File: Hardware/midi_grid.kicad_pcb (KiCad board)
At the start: 2 copper layers, 275 x 200 mm, 329 parts, among them J1 USB_OTG, J2 3.5mm jack, J3 3.5mm jack, J4 Conn_01x04_Male, M1 Mounting_hole, M2 Mounting_hole, M3 Mounting_hole, Q1 BSH205G2, Q10 BSH205G2, Q11 BSH205G2, Q12 BSH205G2, Q13 BSH205G2, Q14 BSH205G2, Q15 BSH205G2, Q16 BSH205G2, Q17 BSH205G2, Q18 BSH205G2, Q19 BSH205G2, Q2 BSH205G2, Q20 BSH205G2, Q21 NX7002AK, Q22 NX7002AK, Q23 NX7002AK, Q24 NX7002AK, Q25 NX7002AK, Q26 NX7002AK, Q27 NX7002AK, Q28 NX7002AK, Q29 NX7002AK, Q3 BSH205G2, Q30 NX7002AK, Q31 NX7002AK, Q32 NX7002AK, Q33 NX7002AK, Q34 NX7002AK, Q4 BSH205G2, Q5 BSH205G2, Q6 BSH205G2, Q7 BSH205G2, Q8 BSH205G2, Q9 BSH205G2, SW1 Button_matrix_4x4, SW10 SW_Push, SW11 SW_Push, SW12 SW_Push, SW13 SW_Push, SW14 SW_Push, SW15 SW_Push, SW16 SW_Push, SW17 SW_Push, SW18 SW_Push, SW19 SW_Push, SW2 Button_matrix_4x4, SW20 SW_Push, SW21 SW_Push, SW22 SW_Push, SW23 SW_Push, SW24 SW_Push, SW25 EC12E24204A9, SW26 EC12E24204A9, SW3 Button_matrix_4x4, SW4 Button_matrix_4x4, SW5 SW_Push, SW6 SW_Push, SW7 SW_Push, SW8 SW_Push, SW9 SW_Push, U1 STM32F411RCT6, U2 74HC138, U3 74HC138, U4 74HC138, U5 USBUF02W6, U6 VO617A, U7 LD1117STR, Y1 8MHz

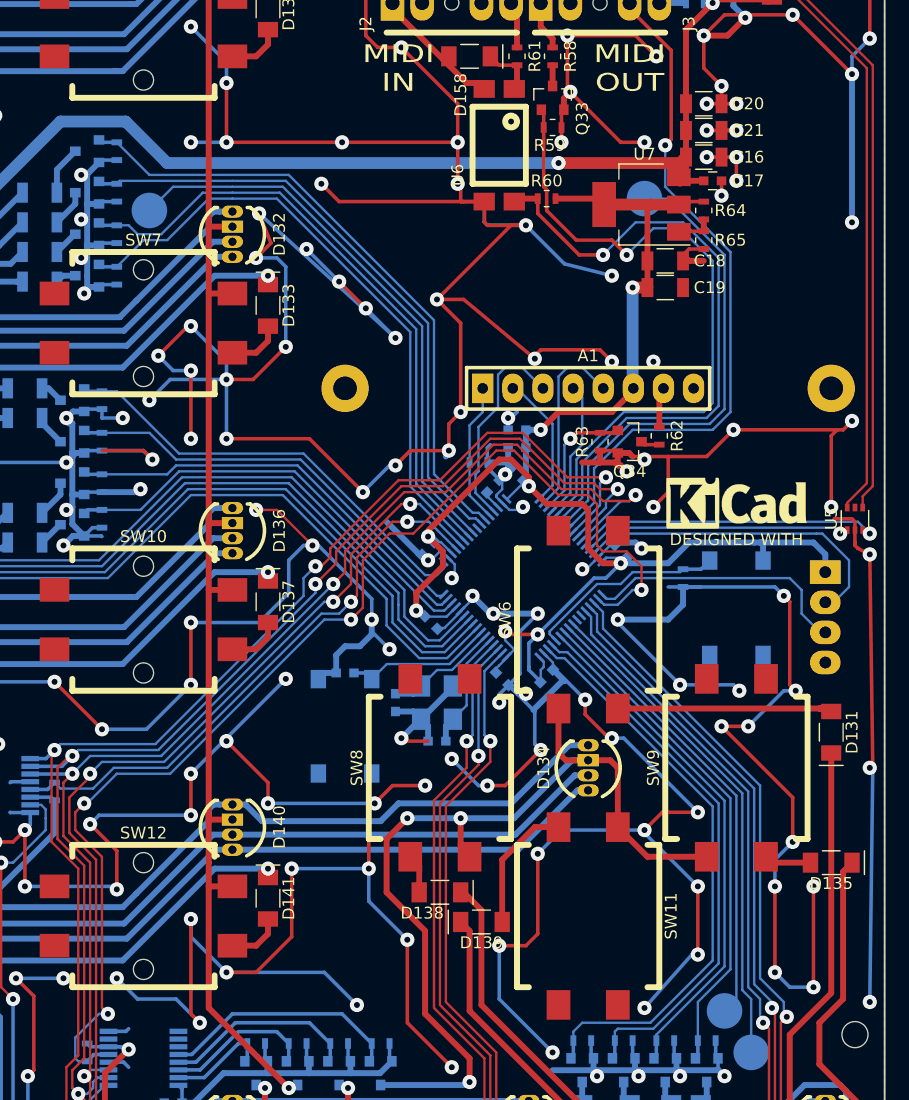
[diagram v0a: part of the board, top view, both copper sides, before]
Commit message: rerouted LCD_LIGHT pin to PB5
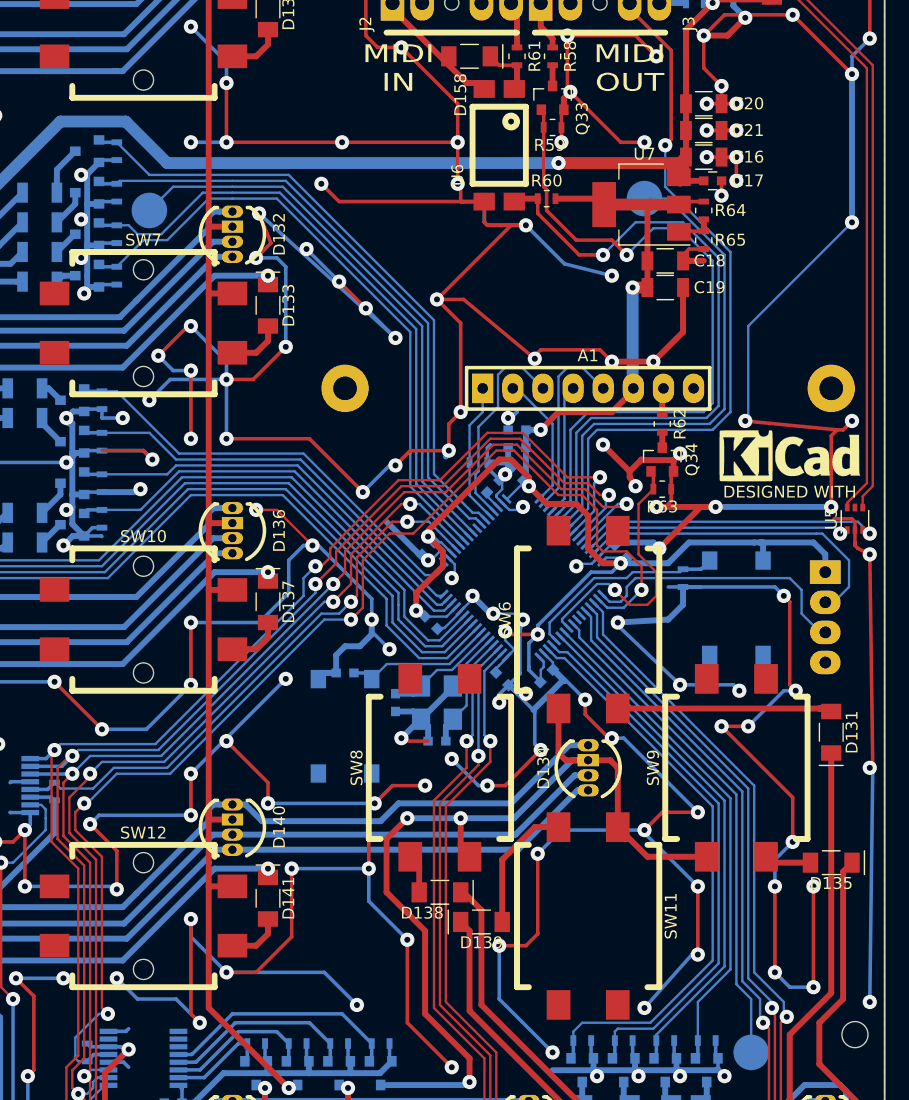
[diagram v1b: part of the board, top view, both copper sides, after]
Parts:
- removed TP3: TEST, project_library:Test_Point_Pad_d3.0mm
- moved R63 6.60 mm to (321.8, 89.0), turned to 0 degrees
- moved GR3 6.02 mm to (332.5, 86.0)
- moved Q34 3.13 mm to (321.8, 86.5), turned to 90 degrees
- moved R62 1.03 mm to (321.8, 83.5)
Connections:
- U1 pad 35: /digital_io/LCD_LIGHT -> Net-(U1-Pad35)
- U1 pad 57: Net-(TP3-Pad1) -> /digital_io/LCD_LIGHT
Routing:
- net GND: track 3945.9 -> 3988.8 mm, vias 317 -> 320
- net Net-(TP3-Pad1): track 37.2 -> 0.00 mm
- net /digital_io/LCD_LIGHT: track 10.6 -> 22.9 mm
- net Net-(TP4-Pad1): track 41.0 -> 42.7 mm
- net /mcu/UART_RX: track 54.0 -> 55.7 mm
- net /mcu/UART_TX: track 57.2 -> 59.0 mm
- net /mcu/MIDI_OUT_DETECT: track 58.3 -> 60.1 mm
- net /mcu/COL3: track 131.4 -> 129.7 mm
- net /mcu/COL2: track 131.1 -> 129.7 mm
- net /mcu/COL1: track 130.9 -> 130.2 mm
- net /mcu/SWDCLK: track 23.4 -> 24.1 mm
- net /digital_io/LCD_MOSI: track 11.8 -> 11.1 mm
- net Net-(A1-Pad7): track 2.89 -> 2.29 mm
- net (no net): vias 1 -> 0

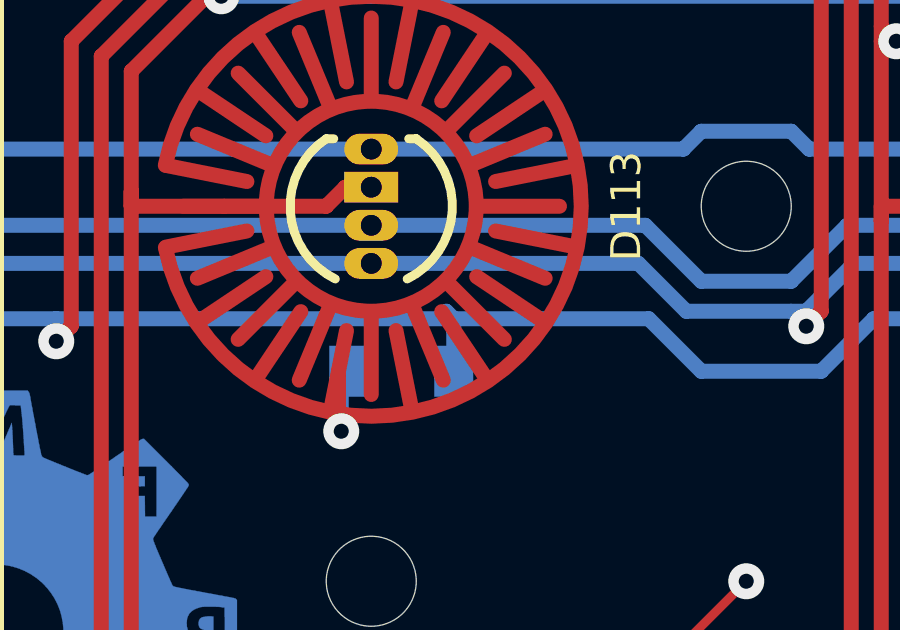
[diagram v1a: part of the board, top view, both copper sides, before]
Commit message: expanded/edited readme files
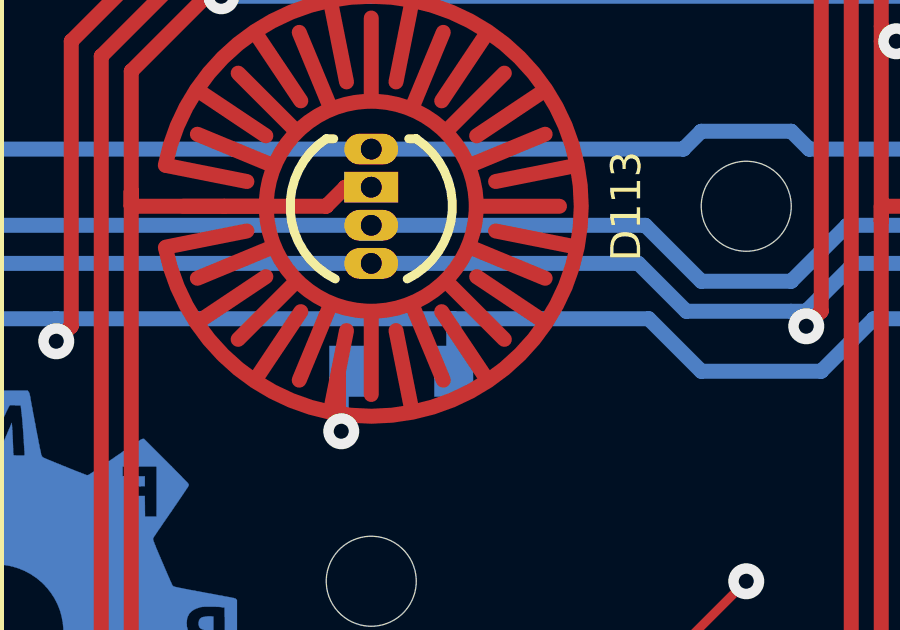
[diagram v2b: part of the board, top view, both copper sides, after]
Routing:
- net /grid/B2: track 715.3 -> 714.7 mm
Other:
- board text added: "Designed by Gediminas Žukaitis Version 1.1 github.com/zukaitis/midi-grid Date of revision: 2018-06-11"
- board text removed: "Designed by Gediminas Žukaitis Version 1.1 github.com/zukaitis/midi-grid Date of revision: 2018-01-27"
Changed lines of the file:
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@@
     (links 866)
     (no_connects 4)
-    (area 65.424999 37.424999 340.575001 237.575001)
+    (area 65.049999 34.025 343.533334 239.275)
     (thickness 1.6)
     (drawings 17)
-    (tracks 4715)
+    (tracks 4713)
     (zones 0)
     (modules 328)
@@
   )
   (setup
-    (last_trace_width 0.2)
+    (last_trace_width 0.5)
     (user_trace_width 0.2)
     (user_trace_width 0.3)
@@
     (effects (font (size 1 1) (thickness 0.2)))
   )
-  (gr_text "Designed by Gediminas Žukaitis\nVersion 1.1\ngithub.com/zukaitis/midi-grid\nDate of revision: 2018-01-27" (at 225.5 214.25) (layer B.SilkS)
+  (gr_text "Designed by Gediminas Žukaitis\nVersion 1.1\ngithub.com/zukaitis/midi-grid\nDate of revision: 2018-06-11" (at 225.5 214.25) (layer B.SilkS)
     (effects (font (size 2 2) (thickness 0.4)) (justify left mirror))
   )
@@
   (segment (start 315.798097 95.298097) (end 314.701903 95.298097) (width 0.2) (layer B.Cu) (net 1))
   (via (at 314.5 95.5) (size 1.2) (drill 0.5) (layers F.Cu B.Cu) (net 1))
-  (segment (start 316.328606 94.767588) (end 315.798097 95.298097) (width 0.2) (layer B.Cu) (net 1) (status 400000))
+  (segment (start 316.328606 94.767588) (end 315.798097 95.298097) (width 0.2) (layer B.Cu) (net 1))
   (segment (start 314.701903 95.298097) (end 314.5 95.5) (width 0.2) (layer B.Cu) (net 1))
   (segment (start 317.5 78.25) (end 321 78.25) (width 0.5) (layer F.Cu) (net 1))
@@
   (segment (start 88 79.5) (end 93 79.5) (width 0.5) (layer B.Cu) (net 222))
   (segment (start 87.25 78.75) (end 88 79.5) (width 0.5) (layer B.Cu) (net 222))
+  (segment (start 180.75 205.5) (end 180.75 203.75) (width 0.5) (layer B.Cu) (net 223))
   (segment (start 230.25 96) (end 169.5 96) (width 0.2) (layer B.Cu) (net 223))
   (segment (start 168 103) (end 168 98) (width 0.5) (layer F.Cu) (net 223))
@@
   (segment (start 230.75 205.5) (end 230.75 203.75) (width 0.5) (layer B.Cu) (net 223))
   (segment (start 205.75 205.5) (end 205.75 203.75) (width 0.5) (layer B.Cu) (net 223))
-  (segment (start 180.75 205.5) (end 180.75 203.75) (width 0.5) (layer B.Cu) (net 223))
-  (segment (start 180.5 203.5) (end 180.5 203.75) (width 0.5) (layer B.Cu) (net 223))
-  (segment (start 180.75 203.75) (end 180.5 203.5) (width 0.5) (layer B.Cu) (net 223))
   (segment (start 305 123) (end 306.5 124.5) (width 0.5) (layer F.Cu) (net 223))
   (segment (start 306.5 132.5) (end 306.5 124.5) (width 0.5) (layer F.Cu) (net 223))
